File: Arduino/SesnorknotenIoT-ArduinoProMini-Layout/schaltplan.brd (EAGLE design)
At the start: 68.2 x 69.8 mm, 10 parts

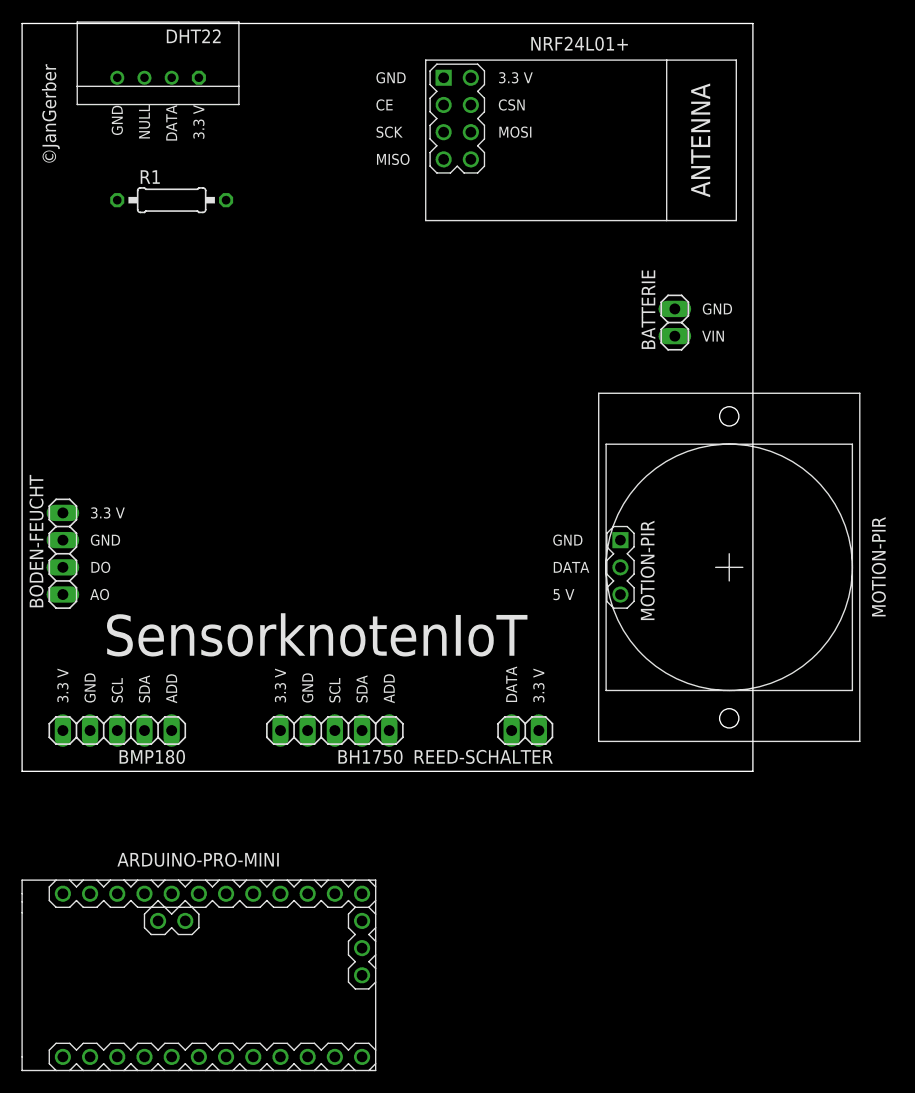
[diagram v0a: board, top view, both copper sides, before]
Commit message: Änderungen Sender Verschlüsselung und Encodierung
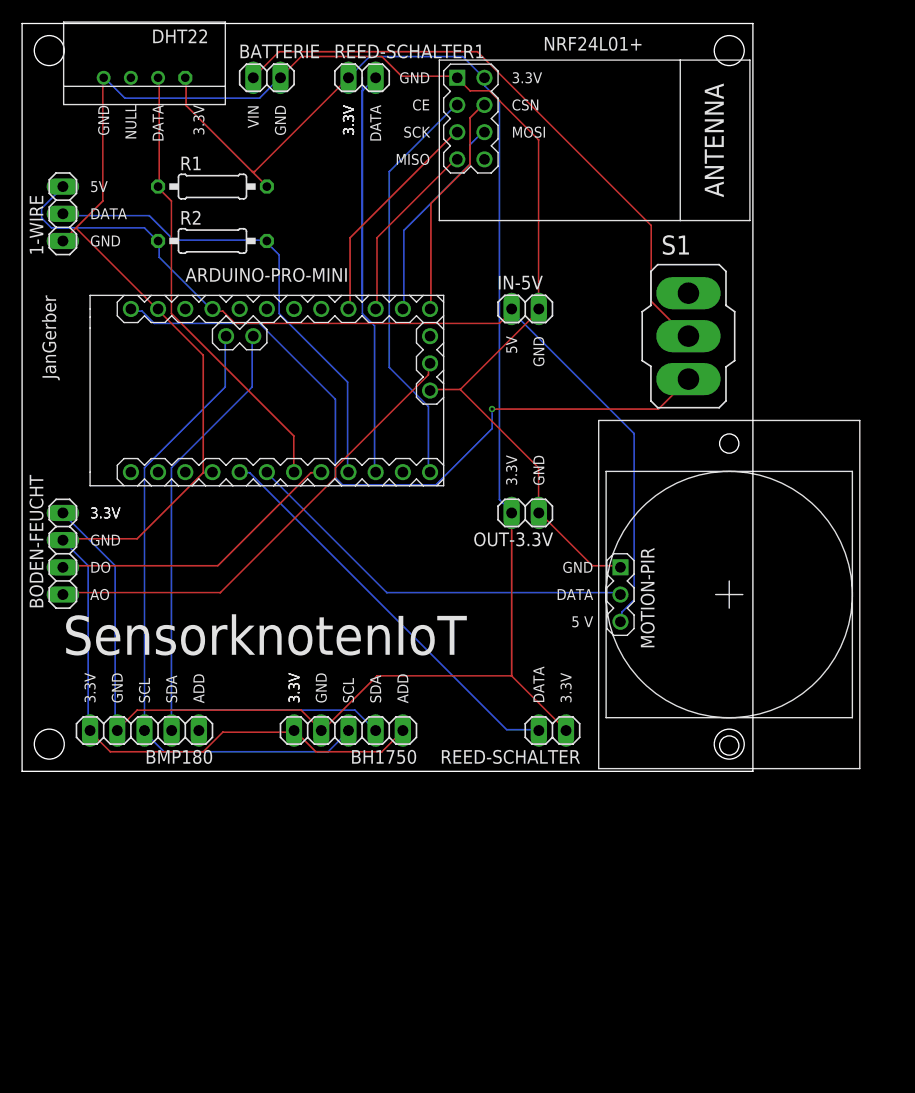
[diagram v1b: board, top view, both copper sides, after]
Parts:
- added 1-WIRE: (no value), pinhead:1X03
- added IN-5V, OUT-3.3V, REED-SCHALTER1: (no value), pinhead:1X02
- added R2: 4k7, resistor:0207/10
- added S1: (no value), switch:320-916
- moved ARDUINO-PRO-MINI 55.0 mm to (22.9, 35.6)
- moved BATTERIE 44.4 mm to (22.9, 64.8), turned to 0 degrees
- moved R1 4.02 mm to (17.8, 54.6)
- moved BMP180 2.54 mm to (11.4, 3.81)
- moved MOTION-PIR 2.54 mm to (66.0, 16.5)
- moved REED-SCHALTER 2.54 mm to (49.5, 3.81)
- moved NRF24L01+ 1.27 mm to (53.3, 58.4)
- moved BH1750 1.27 mm to (30.5, 3.81)
- moved DHT22 1.27 mm to (11.4, 64.8)
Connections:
- removed net GND.1: ARDUINO-PRO-MINI.J7.9
- removed net RAW: ARDUINO-PRO-MINI.J6.1, BATTERIE.1
- removed net VCC: ARDUINO-PRO-MINI.J6.4, MOTION-PIR.3, NRF24L01+.2
- removed net VDD: DHT22.VDD
- new net 3.3V: BH1750.4, BMP180.4, BODEN-FEUCHT.4, DHT22.VDD, NRF24L01+.2, OUT-3.3V.2, R1.2, REED-SCHALTER.1, REED-SCHALTER1.1
- new net IN-3.3V: 1-WIRE.3, ARDUINO-PRO-MINI.J6.4, IN-5V.1, MOTION-PIR.3, R2.1
- new net N$1: ARDUINO-PRO-MINI.J6.1, S1.3
- new net N$10: ARDUINO-PRO-MINI.J7.7, MOTION-PIR.2
- new net N$11: ARDUINO-PRO-MINI.J7.8, REED-SCHALTER.2
- new net N$12: ARDUINO-PRO-MINI.J2.1, BH1750.2, BMP180.2
- new net N$13: ARDUINO-PRO-MINI.J2.2, BH1750.3, BMP180.3
- new net N$15: ARDUINO-PRO-MINI.J7.1, NRF24L01+.3
- new net N$16: ARDUINO-PRO-MINI.J6.12, NRF24L01+.4
- new net N$17: ARDUINO-PRO-MINI.J6.9, NRF24L01+.5
- new net N$18: ARDUINO-PRO-MINI.J6.11, NRF24L01+.6
- new net N$19: ARDUINO-PRO-MINI.J6.10, NRF24L01+.7
- new net N$2: BATTERIE.1, S1.2
- new net N$5: ARDUINO-PRO-MINI.J7.5, BODEN-FEUCHT.2
- new net N$6: ARDUINO-PRO-MINI.J7.6, DHT22.DATA, R1.1
- new net N$7: 1-WIRE.2, ARDUINO-PRO-MINI.J7.4, R2.2
- new net N$8: ARDUINO-PRO-MINI.J3.2, BODEN-FEUCHT.1
- new net N$9: ARDUINO-PRO-MINI.J7.3, REED-SCHALTER1.2
- net GND: now also 1-WIRE.1, ARDUINO-PRO-MINI.J3.1, ARDUINO-PRO-MINI.J7.9, BH1750.5, BMP180.5, IN-5V.2, OUT-3.3V.1; no longer BH1750.4, BMP180.4
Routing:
- net GND: track 0.00 -> 212.5 mm
- net 3.3V: track 0.00 -> 167.4 mm
- net IN-3.3V: track 0.00 -> 87.7 mm
- net N$1: track 0.00 -> 68.4 mm, vias 0 -> 1
- net N$13: track 0.00 -> 60.8 mm
- net N$12: track 0.00 -> 59.8 mm
- net N$9: track 0.00 -> 58.7 mm
- net N$2: track 0.00 -> 57.0 mm
- net N$7: track 0.00 -> 44.9 mm
- net N$8: track 0.00 -> 44.3 mm
- net N$6: track 0.00 -> 42.2 mm
- net N$15: track 0.00 -> 38.6 mm
- net N$11: track 0.00 -> 38.0 mm
- net N$10: track 0.00 -> 37.8 mm
- net N$5: track 0.00 -> 27.8 mm
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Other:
- board text added: "3.3V"
- board text added: "5V"
- board text added: "JanGerber"
- board text removed: "3.3 V"
- board text removed: "©JanGerber"
